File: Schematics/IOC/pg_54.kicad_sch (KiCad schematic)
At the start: 27 parts, among them U5401 PB010, U5402 PB011, U5403 PB012, U5404 PB013, U5405 F20, U5406 F113, U5407 F37, U5408 F37, U5409 F02, U5410 F02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

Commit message: Add workarounds necessary for SystemC simulation.
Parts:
- added U5513, U5514: DELAY, symbol r1000:DELAY
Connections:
- net LOAD_DELAY.S~: now also U5514.2 (OUT); no longer U5419.3 (Q)
- net LOAD_SLICE.S~: now also U5513.2 (OUT); no longer U5418.3 (Q)
- new net: U5419.3 (Q), U5514.1 (In)
- new net: U5418.3 (Q), U5513.1 (In)
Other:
- note added: "Without the delay these signals race Q4~.B1 which clocks the timer chips (TEST_COUNTER_DATA.IOC)"

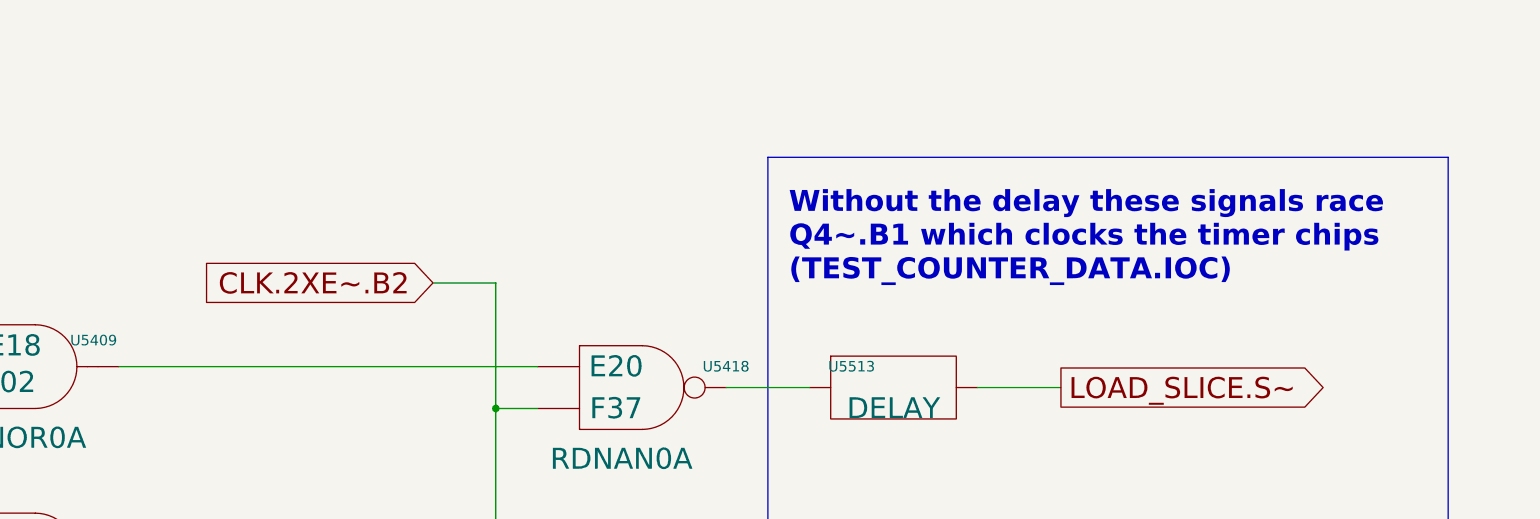
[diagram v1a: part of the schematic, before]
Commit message: Eliminate all multi-buffered signals
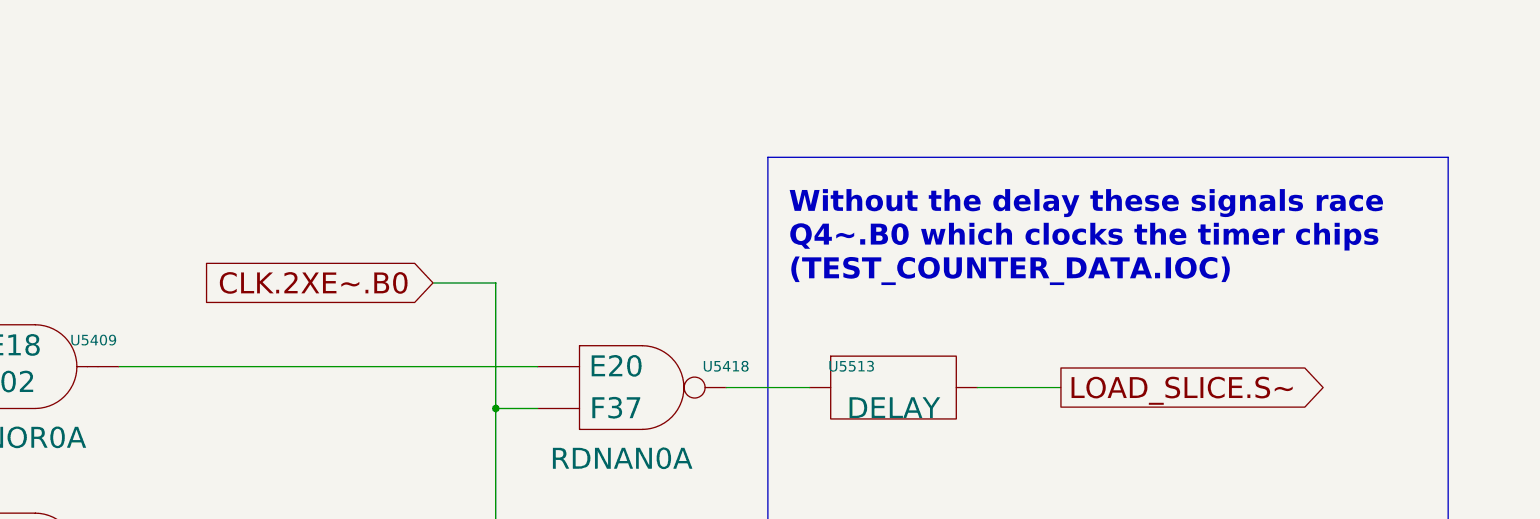
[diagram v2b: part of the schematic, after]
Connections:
- net CLK.2XE~.B2 renamed CLK.2XE~.B0
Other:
- note added: "Without the delay these signals race Q4~.B0 which clocks the timer chips (TEST_COUNTER_DATA.IOC)"
- note removed: "Without the delay these signals race Q4~.B1 which clocks the timer chips (TEST_COUNTER_DATA.IOC)"
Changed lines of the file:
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@@
   )
   (text
-    "Without the delay these signals race\nQ4~.B1 which clocks the timer chips\n(TEST_COUNTER_DATA.IOC)"
+    "Without the delay these signals race\nQ4~.B0 which clocks the timer chips\n(TEST_COUNTER_DATA.IOC)"
     (at 447.04 58.42 0)
     (effects
@@
   )
   (global_label
-    "CLK.2XE~.B2"
+    "CLK.2XE~.B0"
     (shape input)
     (at 403.86 58.42 180)

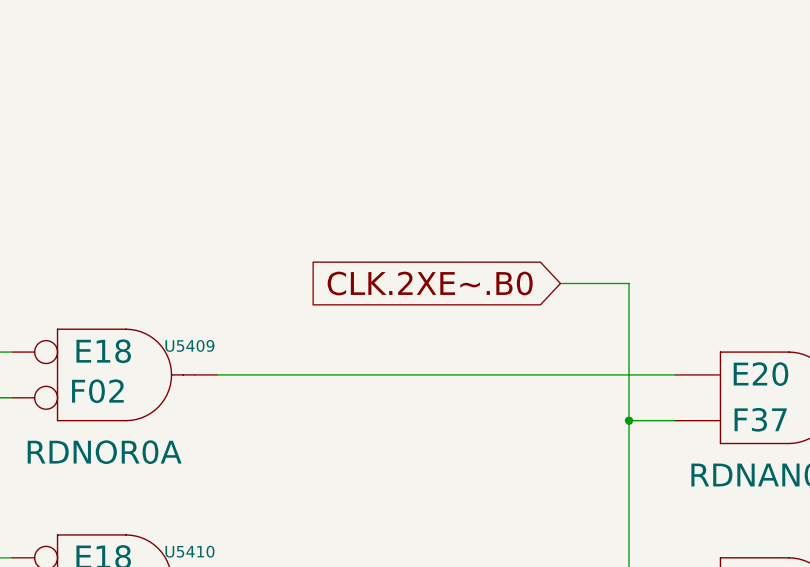
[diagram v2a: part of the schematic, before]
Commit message: Replace lots of clock-generation logic with CLKGEN
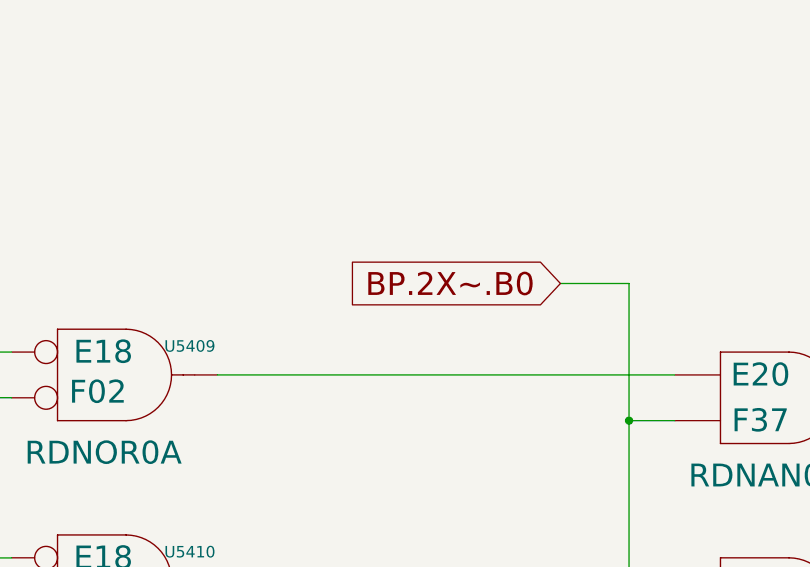
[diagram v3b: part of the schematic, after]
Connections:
- net CLK.2XE~.B0 renamed BP.2X~.B0
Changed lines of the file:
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@@
   )
   (global_label
-    "CLK.2XE~.B0"
+    "BP.2X~.B0"
     (shape input)
     (at 403.86 58.42 180)

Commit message: Reduce RDNAN[01] and MNAN1 activations
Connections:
- net BP.2X~.B0 is gone; now on an unnamed net: U5418.2 (D1), U5419.2 (D1), U5420.2 (D1), U5421.2 (D1), U5422.2 (D1), U5423.2 (D1), U5424.2 (D1), U5425.2 (D1)
- net PD: now also U5409.1 (D0), U5410.1 (D0), U5411.1 (D0), U5412.1 (D0), U5413.1 (D0), U5414.1 (D0), U5415.1 (D0); no longer U5416.2 (D1)
- net STATE_CLK.EN~: no longer U5409.1 (D0), U5410.1 (D0), U5411.1 (D0), U5412.1 (D0), U5413.1 (D0), U5414.1 (D0), U5415.1 (D0)
- new net BP.2X.B0: U5416.2 (D1)
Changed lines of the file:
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@@
   )
   (junction
-    (at 411.48 73.66)
-    (diameter 0)
-    (color 0 0 0 0)
-  )
-  (junction
-    (at 335.28 203.2)
-    (diameter 2.032)
-    (color 0 0 0 0)
-  )
-  (junction
     (at 411.48 96.52)
     (diameter 2.032)
@@
   )
   (junction
+    (at 411.48 228.6)
+    (diameter 0)
+    (color 0 0 0 0)
+  )
+  (junction
     (at 411.48 119.38)
     (diameter 2.032)
@@
   (wire
     (pts
-      (xy 335.28 226.06)
-      (xy 335.28 203.2)
-    )
-    (stroke
-      (width 0)
-      (type solid)
-      (color 0 0 0 0)
-    )
-  )
-  (wire
-    (pts
       (xy 342.9 226.06)
       (xy 335.28 226.06)
@@
   (wire
     (pts
-      (xy 325.12 66.04)
+      (xy 317.5 66.04)
       (xy 335.28 66.04)
     )
@@
   (wire
     (pts
-      (xy 411.48 58.42)
-      (xy 411.48 73.66)
-    )
-    (stroke
-      (width 0)
-      (type solid)
-      (color 0 0 0 0)
-    )
-  )
-  (wire
-    (pts
       (xy 411.48 73.66)
       (xy 411.48 96.52)
@@
   (wire
     (pts
-      (xy 403.86 58.42)
-      (xy 411.48 58.42)
-    )
-    (stroke
-      (width 0)
-      (type default)
-      (color 0 0 0 0)
-    )
-  )
-  (wire
-    (pts
       (xy 256.54 325.12)
       (xy 297.18 325.12)
@@
     (pts
       (xy 411.48 233.68)
-      (xy 411.48 210.82)
+      (xy 411.48 228.6)
     )
     (stroke
@@
   (wire
     (pts
+      (xy 411.48 228.6)
+      (xy 411.48 210.82)
+    )
+    (stroke
+      (width 0)
+      (type solid)
+      (color 0 0 0 0)
+    )
+  )
+  (wire
+    (pts
       (xy 76.2 345.44)
       (xy 109.22 345.44)
@@
   (wire
     (pts
-      (xy 340.36 231.14)
-      (xy 340.36 233.68)
+      (xy 411.48 228.6)
+      (xy 416.56 228.6)
     )
     (stroke
@@
   (wire
     (pts
+      (xy 335.28 231.14)
       (xy 342.9 231.14)
-      (xy 340.36 231.14)
     )
     (stroke
@@
     (pts
       (xy 365.76 228.6)
-      (xy 416.56 228.6)
+      (xy 411.48 228.6)
     )
     (stroke
@@
   )
   (global_label
+    "BP.2X.B0"
+    (shape input)
+    (at 335.28 231.14 180)
+    (fields_autoplaced)
+    (effects
+      (font
+        (size 2.54 2.54)
+      )
+      (justify right)
+    )
+    (property
+      "Intersheet References"
+      "${INTERSHEET_REFS}"
+      (id 0)
+      (at 312.7768 230.9813 0)
+      (effects
+        (font
+          (size 2.54 2.54)
+        )
+        (justify right)
+      )
+    )
+  )
+  (global_label
     "TCB_TOP3"
     (shape output)
@@
     "STATE_CLK.EN~"
     (shape input)
-    (at 325.12 66.04 180)
+    (at 335.28 226.06 180)
     (fields_autoplaced)
     (effects
@@
       "${INTERSHEET_REFS}"
       (id 0)
-      (at 292.475 65.8813 0)
+      (at 302.635 225.9013 0)
       (effects
         (font
@@
   )
   (global_label
-    "BP.2X~.B0"
-    (shape input)
-    (at 403.86 58.42 180)
-    (fields_autoplaced)
-    (effects
-      (font
-        (size 2.54 2.54)
-      )
-      (justify right)
-    )
-    (property
-      "Intersheet References"
-      "${INTERSHEET_REFS}"
-      (id 0)
-      (at 375.5692 58.2613 0)
-      (effects
-        (font
-          (size 2.54 2.54)
-        )
-        (justify right)
-      )
-    )
-  )
-  (global_label
     "DIAG.DUMMY_EN~"
     (shape input)
@@
   )
   (symbol
-    (lib_id "r1000:PD")
-    (at 340.36 233.68 0)
-    (unit 1)
-    (in_bom no)
-    (on_board yes)
-    (property
-      "Reference"
-      "#PWR05405"
-      (id 0)
-      (at 340.36 233.68 0)
-      (effects
-        (font
-          (size 1.27 1.27)
-        )
-        hide
-      )
-    )
-    (property
-      "Value"
-      "PD"
-      (id 1)
-      (at 340.36 233.68 0)
-      (effects
-        (font
-          (size 1.27 1.27)
-        )
-        hide
-      )
-    )
-    (property
-      "Footprint"
-      ""
-      (id 2)
-      (at 340.36 233.68 0)
-      (effects
-        (font
-          (size 1.27 1.27)
-        )
-        hide
-      )
-    )
-    (property
-      "Datasheet"
-      ""
-      (id 3)
-      (at 340.36 233.68 0)
-      (effects
-        (font
-          (size 1.27 1.27)
-        )
-        hide
-      )
-    )
-    (pin
-      "1"
-    )
-  )
-  (symbol
     (lib_id "r1000:PBxxx")
     (at 119.38 215.9 0)
@@
     )
   )
+  (symbol
+    (lib_id "r1000:PD")
+    (at 317.5 66.04 0)
+    (unit 1)
+    (in_bom no)
+    (on_board yes)
+    (property
+      "Reference"
+      "#PWR0123"
+      (id 0)
+      (at 317.5 66.04 0)
+      (effects
+        (font
+          (size 1.27 1.27)
+        )
+        hide
+      )
+    )
+    (property
+      "Value"
+      "PD"
+      (id 1)
+      (at 317.5 66.04 0)
+      (effects
+        (font
+          (size 1.27 1.27)
+        )
+        hide
+      )
+    )
+    (property
+      "Footprint"
+      ""
+      (id 2)
+      (at 317.5 66.04 0)
+      (effects
+        (font
+          (size 1.27 1.27)
+        )
+        hide
+      )
+    )
+    (property
+      "Datasheet"
+      ""
+      (id 3)
+      (at 317.5 66.04 0)
+      (effects
+        (font
+          (size 1.27 1.27)
+        )
+        hide
+      )
+    )
+    (pin
+      "1"
+    )
+  )
